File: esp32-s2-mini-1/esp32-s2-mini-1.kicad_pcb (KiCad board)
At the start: 2 copper layers, 25.4 x 55.2 mm, 20 parts, among them J1 Conn_01x20_Male, J2 USB_C_Receptacle_USB2.0, J3 Conn_01x20_Male, U1 ESP32-S2-MINI, U2 LM1117-3.3

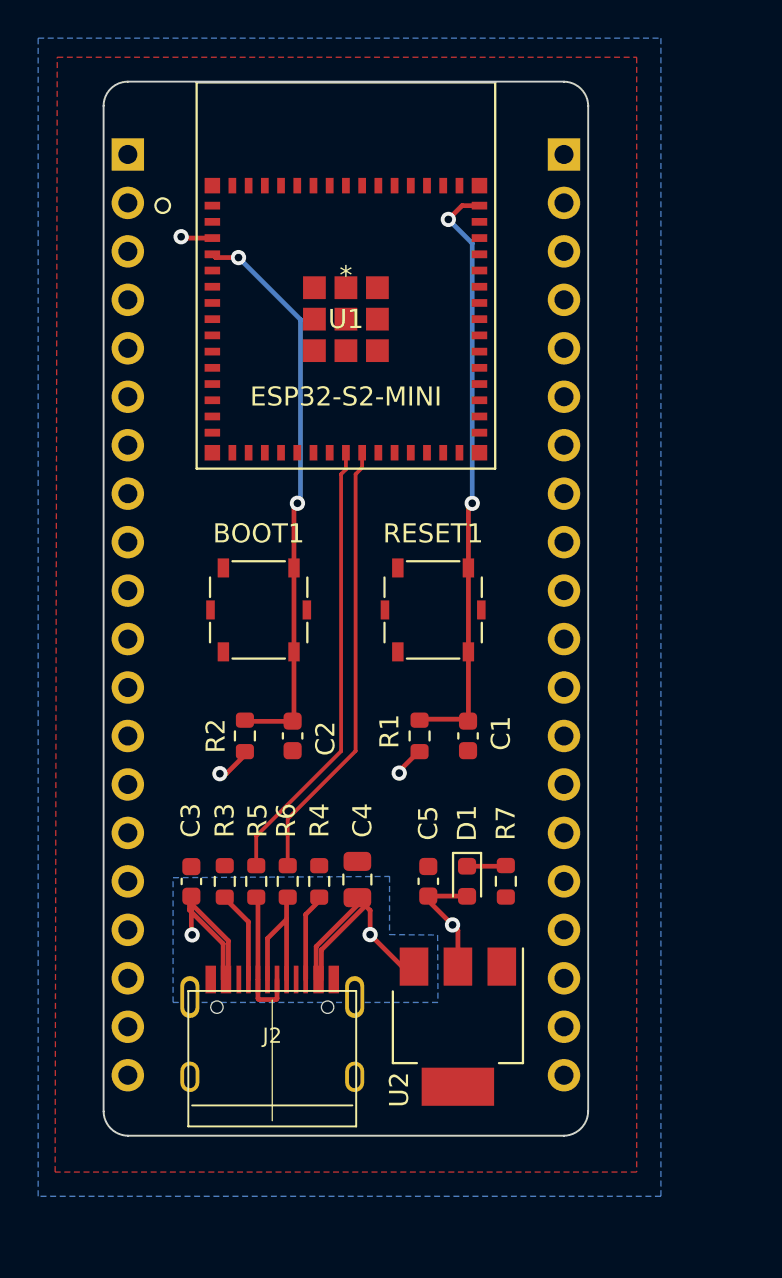
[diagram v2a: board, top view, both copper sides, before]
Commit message: Add controllable LED, dotstar LED, and connect everything
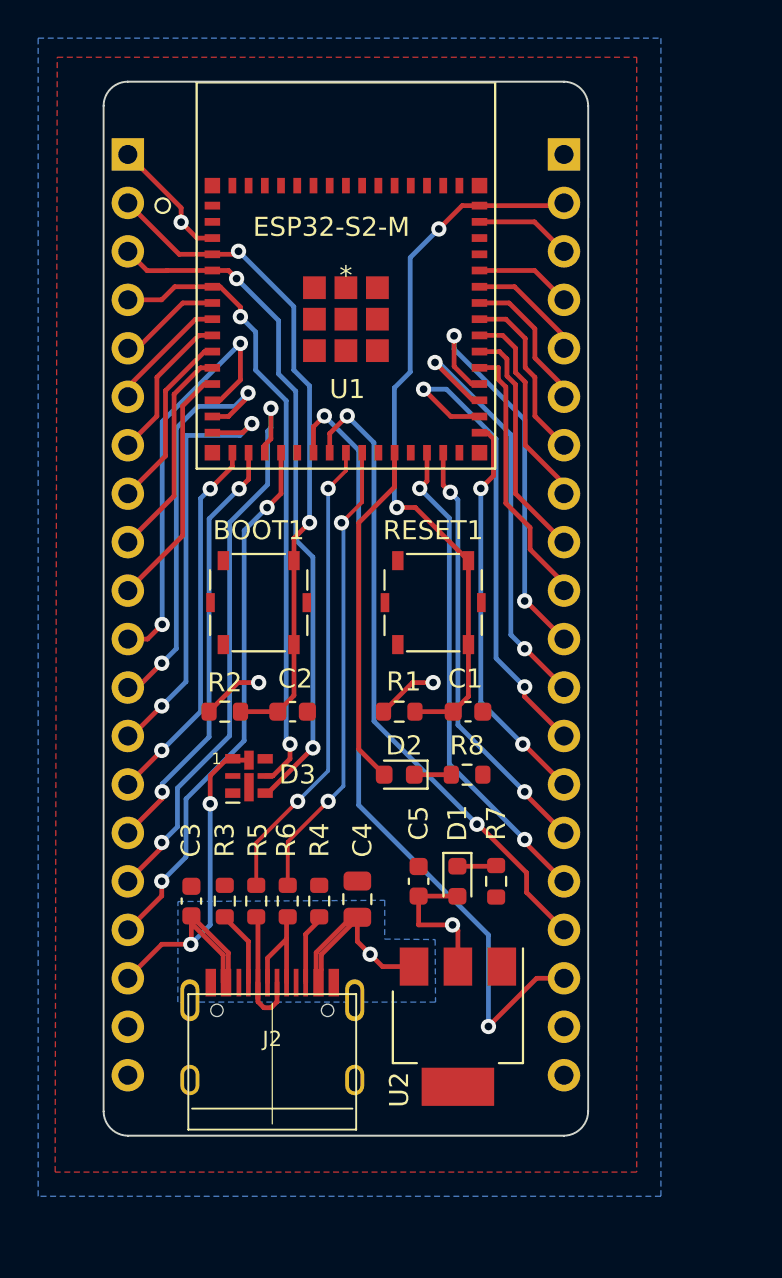
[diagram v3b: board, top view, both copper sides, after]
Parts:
- added D2: LED, LED_SMD:LED_0603_1608Metric, F.Cu at (153.9, 117.6)
- added D3: APA102-2020, LED_SMD:LED-APA102-2020, F.Cu at (146.1, 117.7)
- added R8: 1K, Resistor_SMD:R_0603_1608Metric, F.Cu at (157.5, 117.6)
- U1: value ESP32-S2-MINI -> ESP32-S2-M
- moved R1 1.66 mm to (153.9, 114.3), turned to 180 degrees
- moved R2 1.65 mm to (144.8, 114.3), turned to 180 degrees
- moved C1 1.27 mm to (157.5, 114.3), turned to 180 degrees
- moved C2 1.27 mm to (148.3, 114.3), turned to 180 degrees
- moved C3 1.03 mm to (143.0, 124.2)
- moved C4 1.03 mm to (151.7, 124.1)
- moved R3 1.03 mm to (144.8, 124.2)
- moved R4 1.03 mm to (149.7, 124.2)
- moved R5 1.03 mm to (146.4, 124.2)
- moved R6 1.03 mm to (148.1, 124.2)
- moved C5 0.51 mm to (154.9, 123.2)
- moved R7 0.51 mm to (159.0, 123.2)
- moved D1 0.51 mm to (157.0, 123.2)
- moved BOOT1 0.38 mm to (146.6, 108.6)
- moved RESET1 0.38 mm to (155.7, 108.6)
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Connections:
- J1 pad 1: unconnected-(J1-Pad1) -> +3V3
- J1 pad 10: unconnected-(J1-Pad10) -> Net-(J1-Pad10)
- J1 pad 11: unconnected-(J1-Pad11) -> Net-(J1-Pad11)
- J1 pad 12: unconnected-(J1-Pad12) -> Net-(J1-Pad12)
- J1 pad 13: unconnected-(J1-Pad13) -> Net-(J1-Pad13)
- J1 pad 14: unconnected-(J1-Pad14) -> Net-(J1-Pad14)
- J1 pad 15: unconnected-(J1-Pad15) -> Net-(J1-Pad15)
- J1 pad 16: unconnected-(J1-Pad16) -> Net-(J1-Pad16)
- J1 pad 17: unconnected-(J1-Pad17) -> Net-(J1-Pad17)
- J1 pad 18: unconnected-(J1-Pad18) -> +5V
- J1 pad 19: unconnected-(J1-Pad19) -> GND
- J1 pad 2: unconnected-(J1-Pad2) -> /BOOT
- J1 pad 20: unconnected-(J1-Pad20) -> GND
- J1 pad 3: unconnected-(J1-Pad3) -> /APA_DATA
- J1 pad 4: unconnected-(J1-Pad4) -> /APA_CLOCK
- J1 pad 5: unconnected-(J1-Pad5) -> Net-(J1-Pad5)
- J1 pad 6: unconnected-(J1-Pad6) -> Net-(J1-Pad6)
- J1 pad 7: unconnected-(J1-Pad7) -> Net-(J1-Pad7)
- J1 pad 8: unconnected-(J1-Pad8) -> Net-(J1-Pad8)
- J1 pad 9: unconnected-(J1-Pad9) -> Net-(J1-Pad9)
- J3 pad 1: unconnected-(J3-Pad1) -> GND
- J3 pad 10: unconnected-(J3-Pad10) -> Net-(J3-Pad10)
- J3 pad 11: unconnected-(J3-Pad11) -> Net-(J3-Pad11)
- J3 pad 12: unconnected-(J3-Pad12) -> Net-(J3-Pad12)
- J3 pad 13: unconnected-(J3-Pad13) -> Net-(J3-Pad13)
- J3 pad 14: unconnected-(J3-Pad14) -> Net-(J3-Pad14)
- J3 pad 15: unconnected-(J3-Pad15) -> Net-(J3-Pad15)
- J3 pad 16: unconnected-(J3-Pad16) -> Net-(J3-Pad16)
- J3 pad 17: unconnected-(J3-Pad17) -> Net-(J3-Pad17)
- J3 pad 18: unconnected-(J3-Pad18) -> Net-(J3-Pad18)
- J3 pad 19: unconnected-(J3-Pad19) -> GND
- J3 pad 2: unconnected-(J3-Pad2) -> /ENABLE
- J3 pad 20: unconnected-(J3-Pad20) -> GND
- J3 pad 3: unconnected-(J3-Pad3) -> Net-(J3-Pad3)
- J3 pad 4: unconnected-(J3-Pad4) -> Net-(J3-Pad4)
- J3 pad 5: unconnected-(J3-Pad5) -> /RX
- J3 pad 6: unconnected-(J3-Pad6) -> /TX
- J3 pad 7: unconnected-(J3-Pad7) -> Net-(J3-Pad7)
- J3 pad 8: unconnected-(J3-Pad8) -> Net-(J3-Pad8)
- J3 pad 9: unconnected-(J3-Pad9) -> Net-(J3-Pad9)
- U1 pad 10: unconnected-(U1-Pad10) -> Net-(J1-Pad8)
- U1 pad 11: unconnected-(U1-Pad11) -> Net-(J1-Pad9)
- U1 pad 12: unconnected-(U1-Pad12) -> Net-(J1-Pad10)
- U1 pad 13: unconnected-(U1-Pad13) -> Net-(J1-Pad11)
- U1 pad 14: unconnected-(U1-Pad14) -> Net-(J1-Pad12)
- U1 pad 15: unconnected-(U1-Pad15) -> Net-(J1-Pad13)
- U1 pad 16: unconnected-(U1-Pad16) -> Net-(J1-Pad14)
- U1 pad 17: unconnected-(U1-Pad17) -> Net-(J1-Pad15)
- U1 pad 18: unconnected-(U1-Pad18) -> Net-(J1-Pad16)
- U1 pad 19: unconnected-(U1-Pad19) -> Net-(J1-Pad17)
- U1 pad 21: unconnected-(U1-Pad21) -> Net-(J3-Pad18)
- U1 pad 22: unconnected-(U1-Pad22) -> Net-(J3-Pad17)
- U1 pad 26: unconnected-(U1-Pad26) -> /LED
- U1 pad 28: unconnected-(U1-Pad28) -> Net-(J3-Pad16)
- U1 pad 29: unconnected-(U1-Pad29) -> Net-(J3-Pad15)
- U1 pad 31: unconnected-(U1-Pad31) -> Net-(J3-Pad14)
- U1 pad 32: unconnected-(U1-Pad32) -> Net-(J3-Pad13)
- U1 pad 33: unconnected-(U1-Pad33) -> Net-(J3-Pad12)
- U1 pad 34: unconnected-(U1-Pad34) -> Net-(J3-Pad11)
- U1 pad 35: unconnected-(U1-Pad35) -> Net-(J3-Pad10)
- U1 pad 36: unconnected-(U1-Pad36) -> Net-(J3-Pad9)
- U1 pad 37: unconnected-(U1-Pad37) -> Net-(J3-Pad8)
- U1 pad 38: unconnected-(U1-Pad38) -> Net-(J3-Pad7)
- U1 pad 41: unconnected-(U1-Pad41) -> Net-(J3-Pad4)
- U1 pad 44: unconnected-(U1-Pad44) -> Net-(J3-Pad3)
- U1 pad 5: unconnected-(U1-Pad5) -> /APA_DATA
- U1 pad 6: unconnected-(U1-Pad6) -> /APA_CLOCK
- U1 pad 7: unconnected-(U1-Pad7) -> Net-(J1-Pad5)
- U1 pad 8: unconnected-(U1-Pad8) -> Net-(J1-Pad6)
- U1 pad 9: unconnected-(U1-Pad9) -> Net-(J1-Pad7)
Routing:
- net Net-(J3-Pad18): track 0.00 -> 42.7 mm, vias 0 -> 2
- net /APA_DATA: track 0.00 -> 36.0 mm, vias 0 -> 2
- net Net-(J3-Pad17): track 0.00 -> 34.0 mm, vias 0 -> 2
- net /APA_CLOCK: track 0.00 -> 33.1 mm, vias 0 -> 2
- net Net-(J1-Pad16): track 0.00 -> 30.4 mm, vias 0 -> 2
- net Net-(J1-Pad17): track 0.00 -> 28.3 mm, vias 0 -> 2
- net Net-(J3-Pad16): track 0.00 -> 25.8 mm, vias 0 -> 2
- net Net-(J3-Pad13): track 0.00 -> 25.4 mm, vias 0 -> 2
- net Net-(J3-Pad12): track 0.00 -> 23.1 mm, vias 0 -> 2
- net Net-(J1-Pad13): track 0.00 -> 23.1 mm, vias 0 -> 2
- net Net-(J3-Pad15): track 0.00 -> 22.5 mm, vias 0 -> 2
- net Net-(J1-Pad15): track 0.00 -> 22.5 mm, vias 0 -> 2
- net Net-(J1-Pad11): track 0.00 -> 22.4 mm, vias 0 -> 2
- net Net-(J1-Pad12): track 0.00 -> 22.0 mm, vias 0 -> 2
- net Net-(J3-Pad11): track 0.00 -> 21.6 mm, vias 0 -> 2
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
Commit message: Adding labels to pins in the schematic
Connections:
- net /APA_CLOCK renamed /IO2_APA_CLK
- net /APA_DATA renamed /IO1_APA_DTA
- net /BOOT renamed /IO0_BOOT
- net /ENABLE renamed /RESET
- net /LED renamed /IO26_LED
- net Net-(J1-Pad10) renamed /IO8
- net Net-(J1-Pad11) renamed /IO9
- net Net-(J1-Pad12) renamed /IO10
- net Net-(J1-Pad13) renamed /IO11
- net Net-(J1-Pad14) renamed /IO12
- net Net-(J1-Pad15) renamed /IO13
- net Net-(J1-Pad16) renamed /IO14
- net Net-(J1-Pad17) renamed /IO15
- net Net-(J1-Pad5) renamed /IO3
- net Net-(J1-Pad6) renamed /IO4
- net Net-(J1-Pad7) renamed /IO5
- net Net-(J1-Pad8) renamed /IO6
- net Net-(J1-Pad9) renamed /IO7
- net Net-(J3-Pad10) renamed /IO39
- net Net-(J3-Pad11) renamed /IO38
- net Net-(J3-Pad12) renamed /IO37
- net Net-(J3-Pad13) renamed /IO36
- net Net-(J3-Pad14) renamed /IO35
- net Net-(J3-Pad15) renamed /IO34
- net Net-(J3-Pad16) renamed /IO33
- net Net-(J3-Pad17) renamed /IO18
- net Net-(J3-Pad18) renamed /IO17
- net Net-(J3-Pad3) renamed /IO46
- net Net-(J3-Pad4) renamed /IO45
- net Net-(J3-Pad7) renamed /IO42
- net Net-(J3-Pad8) renamed /IO41
- net Net-(J3-Pad9) renamed /IO40

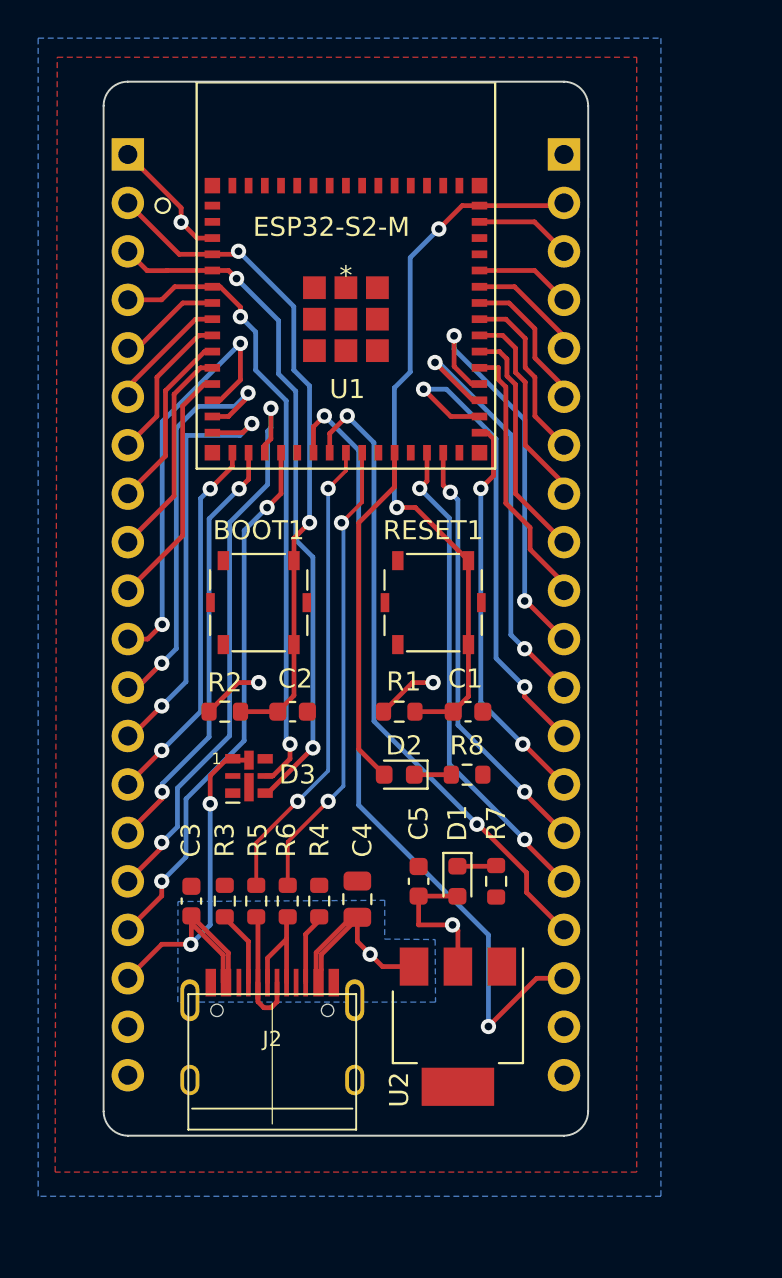
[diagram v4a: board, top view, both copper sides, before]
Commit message: Adding labels to half the pins on the pcb front
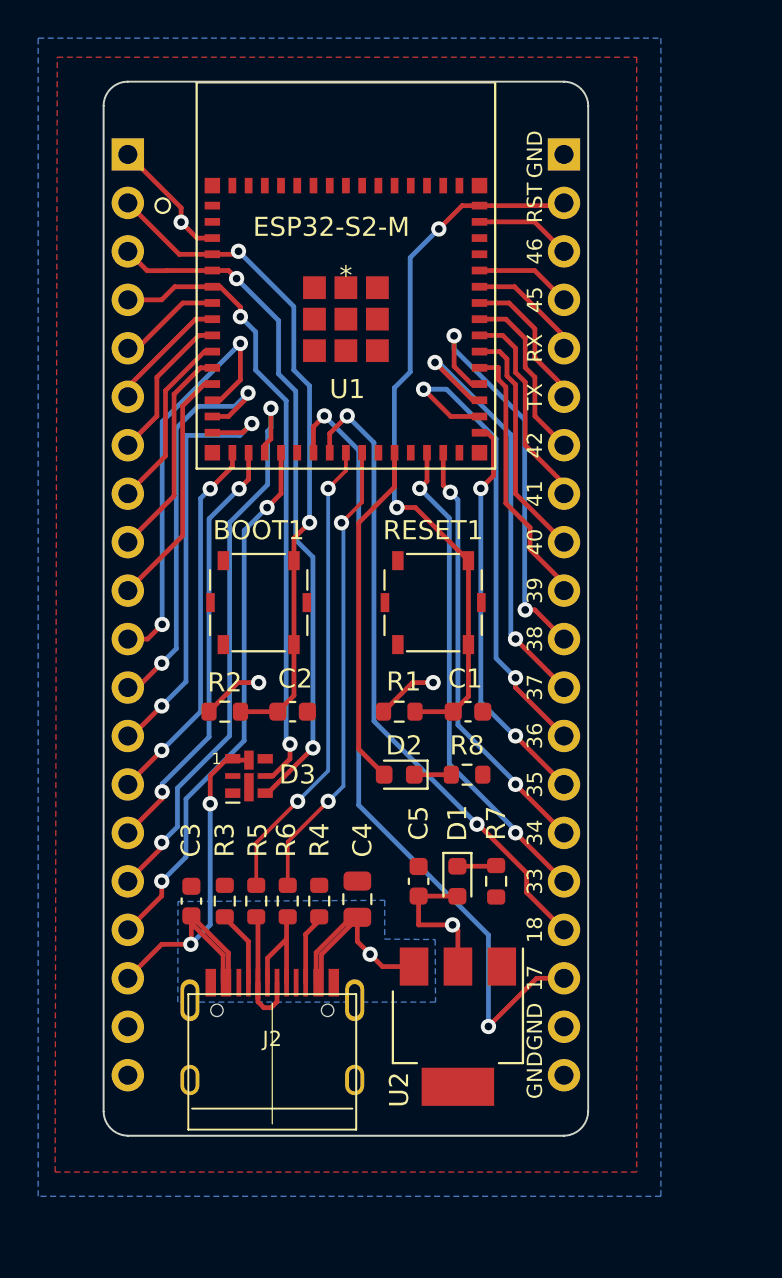
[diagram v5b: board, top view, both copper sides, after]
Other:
- board text added: "17"
- board text added: "18"
- board text added: "33"
- board text added: "34"
- board text added: "35"
- board text added: "36"
- board text added: "37"
- board text added: "38"
- board text added: "39"
- board text added: "40"
- board text added: "41"
- board text added: "42"
- board text added: "45"
- board text added: "46"
- board text added: "GND"
- board text added: "RST"
- board text added: "RX"
- board text added: "TX"

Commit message: Adding labels to the other half the pins on the pcb front
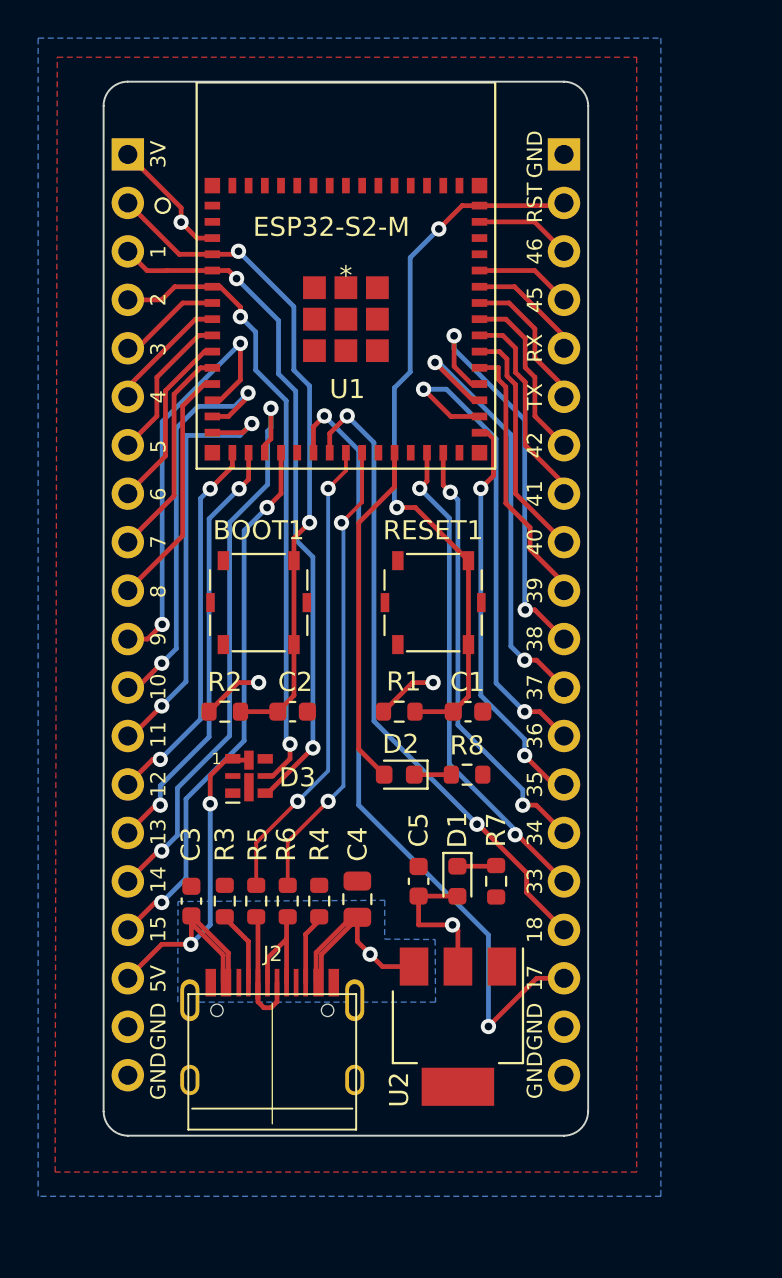
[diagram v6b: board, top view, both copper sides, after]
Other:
- board text added: "1"
- board text added: "10"
- board text added: "11"
- board text added: "12"
- board text added: "13"
- board text added: "14"
- board text added: "15"
- board text added: "2"
- board text added: "3"
- board text added: "3V"
- board text added: "4"
- board text added: "5"
- board text added: "5V"
- board text added: "6"
- board text added: "7"
- board text added: "8"
- board text added: "9"
